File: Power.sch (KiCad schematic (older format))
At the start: 38 parts, among them IC3 INA181A1, IC4 INA181A1, IC5 INA181A1, U2 IRS2186, U3 IRS2186, U4 IRS2186

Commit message: - removed lots of unused circuitry - implemented new DMOS power stage - power supplies still missing - removed rescue lib and fixed referenced
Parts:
- removed C33, C35, C4, C43, C44, C5, C6, C7, C8: 1u, Capacitor_SMD:C_0805_2012Metric, symbol Device:C
- removed C34, C39, C41: 10n, Capacitor_SMD:C_0805_2012Metric, symbol Device:C
- removed C36, C40, C42: 100n, Capacitor_SMD:C_0805_2012Metric, symbol Device:C
- removed D1, D5, D6: BAS21L, Diode_SMD:D_SOT-23_ANK, symbol Device:D_Small
- removed D11, D12: 3V3, Diode_SMD:D_SOD-123, symbol Revolter-rescue:ZENER-RESCUE-Revolter
- removed IC3, IC4, IC5: INA181A1, Package_TO_SOT_SMD:SOT-23-6, symbol Revolter-rescue:INA181
- removed R3, R47, R48: WSLF2512L5000FEB, Resistor_SMD:R_2512_6332Metric, symbol Device:R
- removed R45, R46: 1k, Resistor_SMD:R_0805_2012Metric, symbol Device:R
- removed R55, R57: 100k, Resistor_SMD:R_0805_2012Metric, symbol Revolter-rescue:R-RESCUE-BLDC_4
- removed R56, R58: 3k3, Resistor_SMD:R_0805_2012Metric, symbol Revolter-rescue:R-RESCUE-BLDC_4
- removed U2, U3, U4: IRS2186, Package_SO:SO-8_3.9x4.9mm_P1.27mm, symbol Revolter-rescue:IRS2186-Driver_FET
- added C? (x6): 1u, symbol Device:C
- added C? (x3): 1n, symbol Device:C
- added D? (x3): D, symbol Device:D
- added D? (x2): 3V3, Diode_SMD:D_SOD-123, symbol Device:D_Zener
- added IC? (x3): IRSM005, symbol Revolterlib:IRSM005
- added R? (x6): 1R, Resistor_SMD:R_0805_2012Metric, symbol Device:R
- added R? (x2): 100k, Resistor_SMD:R_0805_2012Metric, symbol Device:R
- added R? (x2): 3k3, Resistor_SMD:R_0805_2012Metric, symbol Device:R
- added U? (x3): ACS730xLCTR-50AB, Package_SO:SOIC-8_3.9x4.9mm_P1.27mm, symbol Sensor_Current:ACS730xLCTR-50AB
- D10: symbol Revolter-rescue:ZENER-RESCUE-Revolter -> Device:D_Zener
- R53, R54: symbol Revolter-rescue:R-RESCUE-BLDC_4 -> Device:R
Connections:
- net labels added: +BATT, CURRENT_U, CURRENT_V, CURRENT_W, HU, HV, HW, LU, LV, LW, Phase_U, Phase_V, Phase_W, VOLTAGE_V, VOLTAGE_W
- net labels removed: +12V, CURRENT_1, CURRENT_2, CURRENT_3, H1, H1_LOW, H1_VS, H2, H2_LOW, H2_VS, H3, H3_LOW, H3_VS, L1, L2, L3, M_H1, M_H2, M_H3, M_L1, M_L2, M_L3, U/2, VOLTAGE_1, VOLTAGE_2, VOLTAGE_3
- wire segments 91 -> 24
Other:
- note removed: "MCU must sense the\nvoltage at each phase"

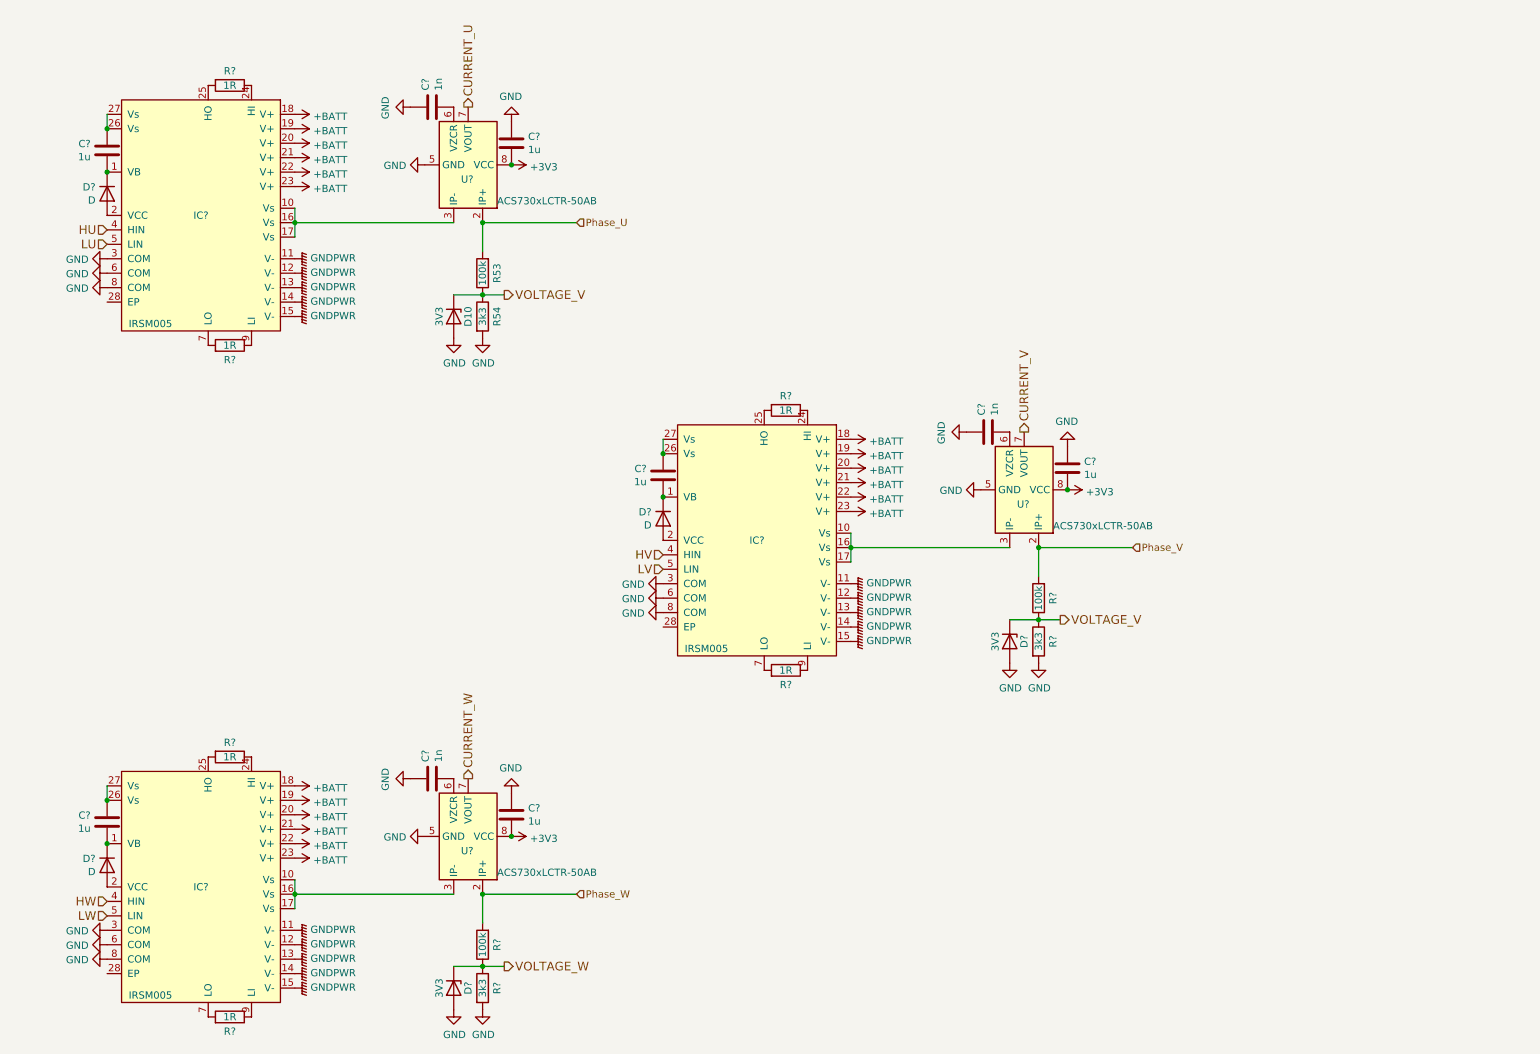
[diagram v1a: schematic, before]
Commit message: - fixed ACS730 pin issue - added power supplies - added footprint library - added footprint for IRSM005
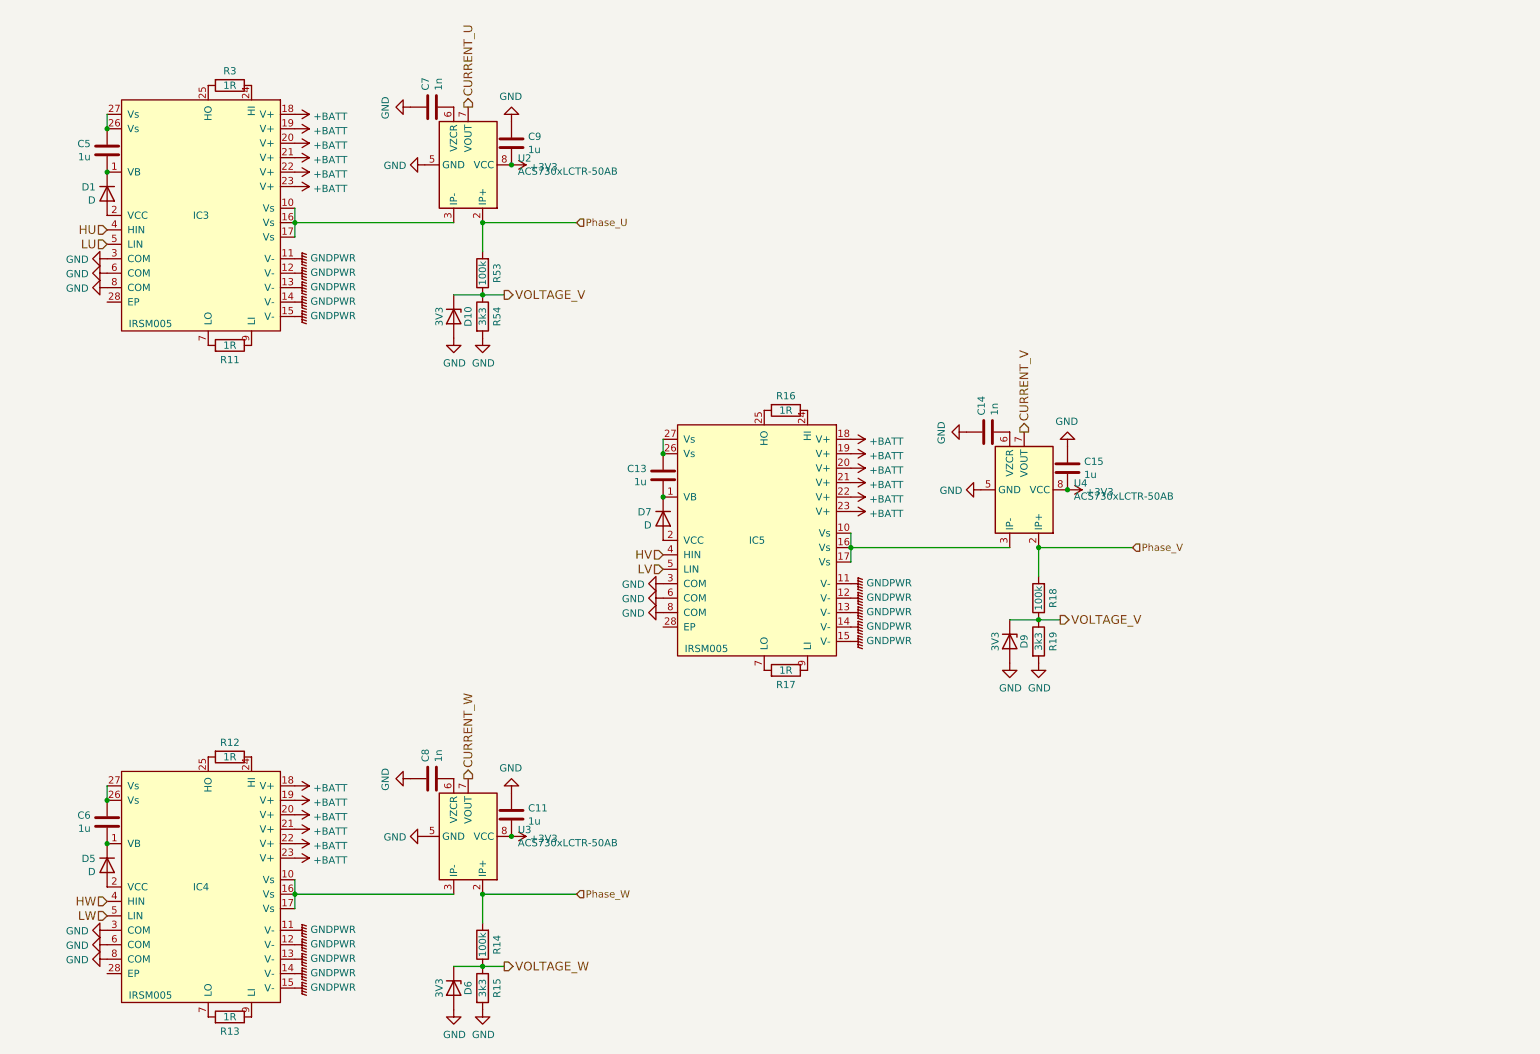
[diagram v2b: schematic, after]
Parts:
- removed U? (x3): ACS730xLCTR-50AB, Package_SO:SOIC-8_3.9x4.9mm_P1.27mm, symbol Sensor_Current:ACS730xLCTR-50AB
- added U2, U3, U4: ACS730xLCTR-50AB, Package_SO:SOIC-8_3.9x4.9mm_P1.27mm, symbol Revolterlib:ACS730xLCTR-50AB
- C11, C13, C14, C15, C5, C6, C7, C8, C9: renamed from C?; footprint (none) -> Capacitor_SMD:C_0805_2012Metric
- D1, D5, D7: renamed from D?; footprint (none) -> Diode_SMD:D_SOD-123
- IC3, IC4, IC5: renamed from IC?; footprint (none) -> Revolter_100V:IRSM005
- gave numbers to parts that had none: 12
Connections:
- net +3V3: now also U2.8 (VCC), U3.8 (VCC), U4.8 (VCC)
- net CURRENT_U: now also U2.7 (VOUT)
- net CURRENT_V: now also U4.7 (VOUT)
- net CURRENT_W: now also U3.7 (VOUT)
- net GND: now also U2.5 (GND), U3.5 (GND), U4.5 (GND)
- net Phase_U: now also U2.1 (IP+), U2.2 (IP+)
- net Phase_V: now also U4.1 (IP+), U4.2 (IP+)
- net Phase_W: now also U3.1 (IP+), U3.2 (IP+)
- net at IC3.10 (Vs), IC3.16 (Vs), IC3.17 (Vs): now also U2.3 (IP-), U2.4 (IP-)
- net at IC5.10 (Vs), IC5.16 (Vs), IC5.17 (Vs): now also U4.3 (IP-), U4.4 (IP-)
- net at IC4.10 (Vs), IC4.16 (Vs), IC4.17 (Vs): now also U3.3 (IP-), U3.4 (IP-)
- net at C7.1: now also U2.6 (VZCR)
- net at C8.1: now also U3.6 (VZCR)
- net at C14.1: now also U4.6 (VZCR)

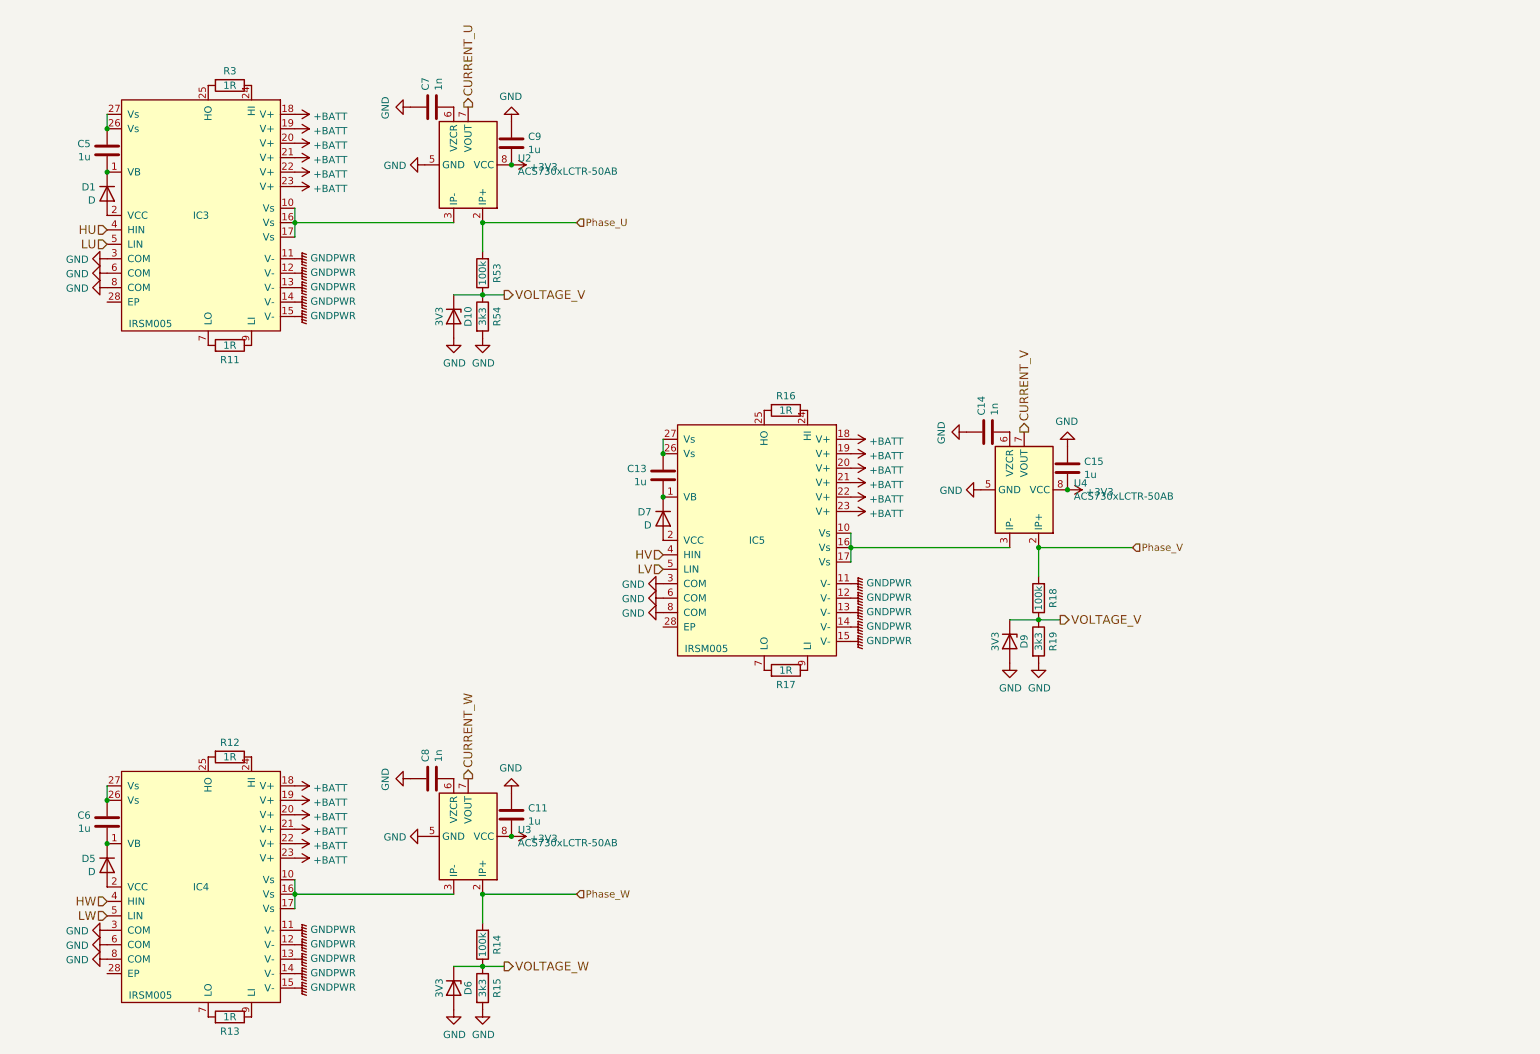
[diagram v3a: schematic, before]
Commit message: - did most of the layout
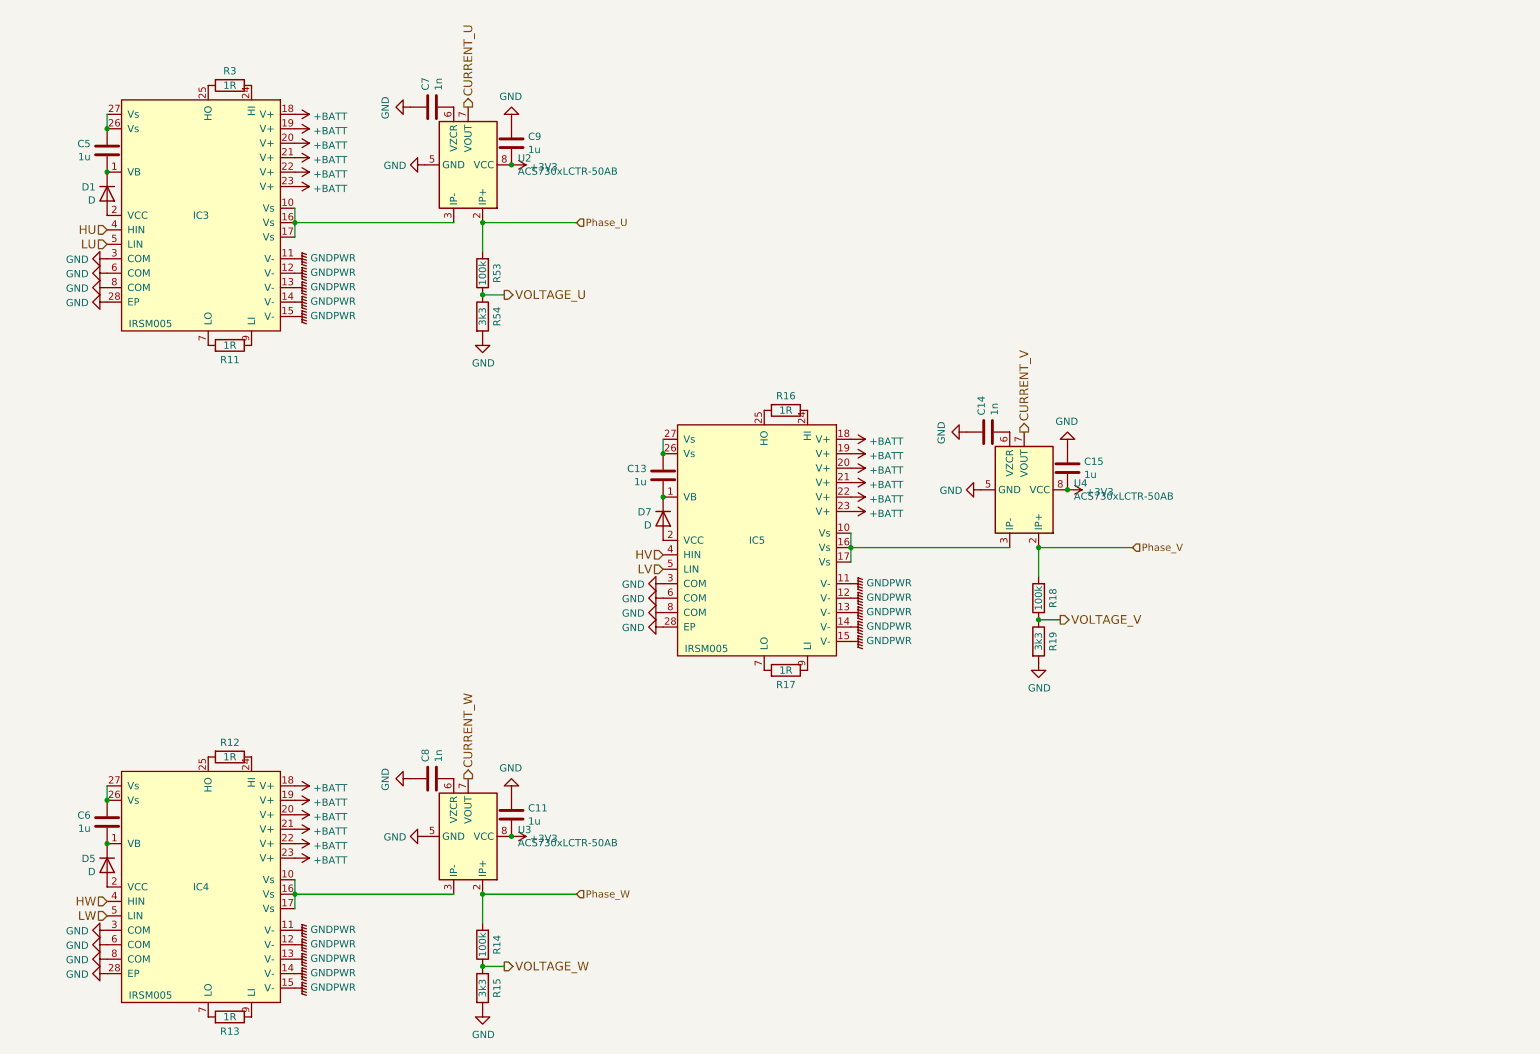
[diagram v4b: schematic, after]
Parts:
- removed D10, D6, D9: 3V3, Diode_SMD:D_SOD-123, symbol Device:D_Zener
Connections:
- net GND: now also IC3.28 (EP), IC4.28 (EP), IC5.28 (EP)
- net VOLTAGE_V: no longer R53.1, R54.1
- new net VOLTAGE_U: R53.1, R54.1
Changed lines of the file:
@@
 VOLTAGE_V
 Text HLabel 3950 2450 2    60   Output ~ 0
-VOLTAGE_V
+VOLTAGE_U
 Text HLabel 3950 7100 2    60   Output ~ 0
 VOLTAGE_W
@@
 CURRENT_W
 $Comp
-L Device:D_Zener D10
-U 1 1 599A646A
-P 3600 2600
-F 0 "D10" H 3600 2700 50  0000 C CNN
-F 1 "3V3" H 3600 2500 50  0000 C CNN
-F 2 "Diode_SMD:D_SOD-123" H 3600 2600 50  0001 C CNN
-F 3 "" H 3600 2600 50  0000 C CNN
-	1    3600 2600
-	0    1    1    0
-$EndComp
-$Comp
 L Device:R R3
 U 1 1 5EE913CC
@@
 	1    0    0    -1
 $EndComp
-Wire Wire Line
-	3600 2450 3800 2450
-$Comp
-L power:GND #PWR0164
-U 1 1 5EF03DF6
-P 3600 2750
-F 0 "#PWR0164" H 3600 2500 50  0001 C CNN
-F 1 "GND" H 3605 2577 50  0000 C CNN
-F 2 "" H 3600 2750 50  0001 C CNN
-F 3 "" H 3600 2750 50  0001 C CNN
-	1    3600 2750
-	1    0    0    -1
-$EndComp
-$Comp
-L Device:D_Zener D6
-U 1 1 5EF04D16
-P 3600 7250
-F 0 "D6" H 3600 7350 50  0000 C CNN
-F 1 "3V3" H 3600 7150 50  0000 C CNN
-F 2 "Diode_SMD:D_SOD-123" H 3600 7250 50  0001 C CNN
-F 3 "" H 3600 7250 50  0000 C CNN
-	1    3600 7250
-	0    1    1    0
-$EndComp
-Wire Wire Line
-	3600 7100 3800 7100
-$Comp
-L power:GND #PWR0165
-U 1 1 5EF04D1D
-P 3600 7400
-F 0 "#PWR0165" H 3600 7150 50  0001 C CNN
-F 1 "GND" H 3605 7227 50  0000 C CNN
-F 2 "" H 3600 7400 50  0001 C CNN
-F 3 "" H 3600 7400 50  0001 C CNN
-	1    3600 7400
-	1    0    0    -1
-$EndComp
 Text HLabel 8300 4200 2    50   Input ~ 0
 Phase_V
@@
 	1    0    0    -1
 $EndComp
-$Comp
-L Device:D_Zener D9
-U 1 1 5EF63640
-P 7450 4850
-F 0 "D9" H 7450 4950 50  0000 C CNN
-F 1 "3V3" H 7450 4750 50  0000 C CNN
-F 2 "Diode_SMD:D_SOD-123" H 7450 4850 50  0001 C CNN
-F 3 "" H 7450 4850 50  0000 C CNN
-	1    7450 4850
-	0    1    1    0
-$EndComp
 Wire Wire Line
 	7450 4200 6350 4200
@@
 Wire Wire Line
 	8300 4200 7650 4200
-Wire Wire Line
-	7450 4700 7650 4700
-$Comp
-L power:GND #PWR0175
-U 1 1 5EF6366B
-P 7450 5000
-F 0 "#PWR0175" H 7450 4750 50  0001 C CNN
-F 1 "GND" H 7455 4827 50  0000 C CNN
-F 2 "" H 7450 5000 50  0001 C CNN
-F 3 "" H 7450 5000 50  0001 C CNN
-	1    7450 5000
-	1    0    0    -1
-$EndComp
 $Comp
 L Device:C C14
@@
 Wire Wire Line
 	3800 6600 4450 6600
+$Comp
+L power:GND #PWR?
+U 1 1 5EF3D8E8
+P 1200 2500
+F 0 "#PWR?" H 1200 2250 50  0001 C CNN
+F 1 "GND" V 1205 2372 50  0000 R CNN
+F 2 "" H 1200 2500 50  0001 C CNN
+F 3 "" H 1200 2500 50  0001 C CNN
+	1    1200 2500
+	0    1    1    0
+$EndComp
+$Comp
+L power:GND #PWR?
+U 1 1 5EF3DB29
+P 5050 4750
+F 0 "#PWR?" H 5050 4500 50  0001 C CNN
+F 1 "GND" V 5055 4622 50  0000 R CNN
+F 2 "" H 5050 4750 50  0001 C CNN
+F 3 "" H 5050 4750 50  0001 C CNN
+	1    5050 4750
+	0    1    1    0
+$EndComp
+$Comp
+L power:GND #PWR?
+U 1 1 5EF3ECF4
+P 1200 7150
+F 0 "#PWR?" H 1200 6900 50  0001 C CNN
+F 1 "GND" V 1205 7022 50  0000 R CNN
+F 2 "" H 1200 7150 50  0001 C CNN
+F 3 "" H 1200 7150 50  0001 C CNN
+	1    1200 7150
+	0    1    1    0
+$EndComp
 $EndSCHEMATC
